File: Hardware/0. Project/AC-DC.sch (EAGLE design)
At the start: 0 parts

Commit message: Schematic design started
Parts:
- added B1, B2: (no value), rectifier:GBPC1
- added C1, C5: 15.000uF x 50V, rcl:CPOL-EUE10-35
- added C2, C6: 100nF x 50V, rcl:C-EU025-025X050
- added C3, C4, C7, C8: 10uF x 50V, rcl:CPOL-EUE3.5-8
- added D1, D2, D3, D4: 1N4007, diode:1N5060GP
- added F1: (no value), fuse:19559
- added R1, R3: (no value), rcl:R-EU_0207/7
- added R2, R4: (no value), pot:3RP/1610N
- added TR?1, TR?2: TRAFO, Trafo:TRAFO
- added U$1, U$4: AMMETER, Instrumentos:AMMETER
- added U$2, U$5: VOLTMETER, Instrumentos:VOLTMETER
- added U$3: GENERATOR, Instrumentos:GENERATOR
- added U1, U2: LM338K, REG1117:REG1117F
- added X1: (no value), con-ptr500:AK500/4-H
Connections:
- new net N$1: B1.AC1, TR?1.GRN@1
- new net N$10: F1.2, TR?1.BLK@1
- new net N$11: B2.AC1, TR?2.GRN@1
- new net N$12: B2.AC2, TR?2.GRN@2
- new net N$13: B2.+, C5.+, C6.1, D4.C, U2.VIN
- new net N$14: B2.-, C5.-, C6.2, C7.-, C8.-, R4.A, R4.S, U$5.P$2, X1-3.KL
- new net N$15: C8.+, D3.C, D4.A, R3.2, U$4.P$3, U2.VOUT
- new net N$16: C7.+, D3.A, R3.1, R4.E, U2.GND
- new net N$17: U$4.P$2, U$5.P$3, X1-4.KL
- new net N$18: TR?2.GRN/YEL1
- new net N$19: TR?2.BLK@1
- new net N$2: B1.AC2, TR?1.GRN@2
- new net N$3: B1.+, C1.+, C2.1, D2.C, U1.VIN
- new net N$4: B1.-, C1.-, C2.2, C3.-, C4.-, R2.A, R2.S, U$2.P$2, X1-2.KL
- new net N$5: C4.+, D1.C, D2.A, R1.2, U$1.P$3, U1.VOUT
- new net N$6: C3.+, D1.A, R1.1, R2.E, U1.GND
- new net N$7: U$1.P$2, U$2.P$3, X1-1.KL
- new net N$8: F1.1, U$3.P$3
- new net N$9: TR?1.GRN/YEL1, U$3.P$2

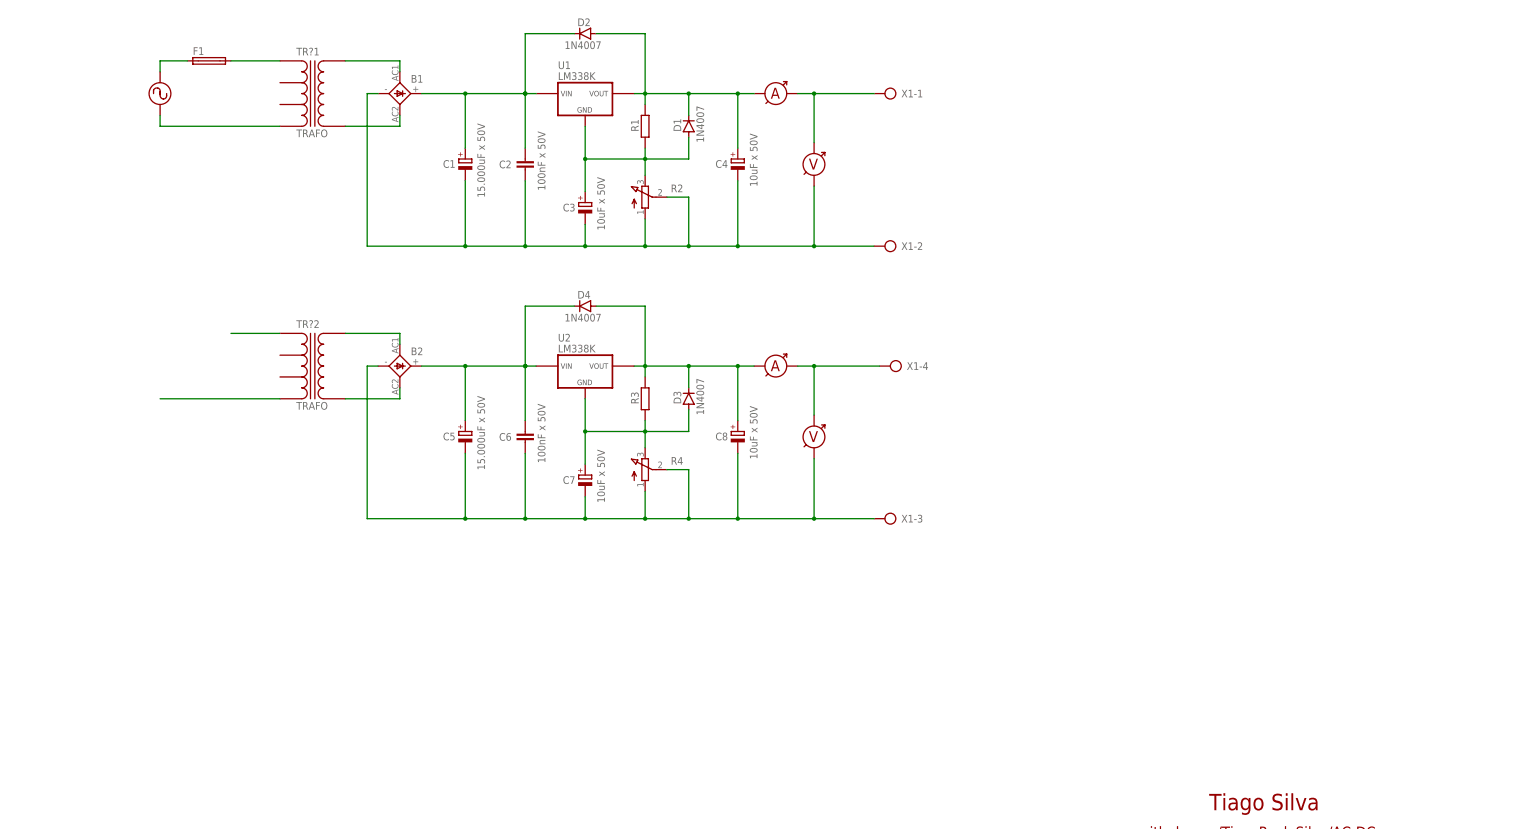
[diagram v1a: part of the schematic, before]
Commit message: Short-circuit added to schematic
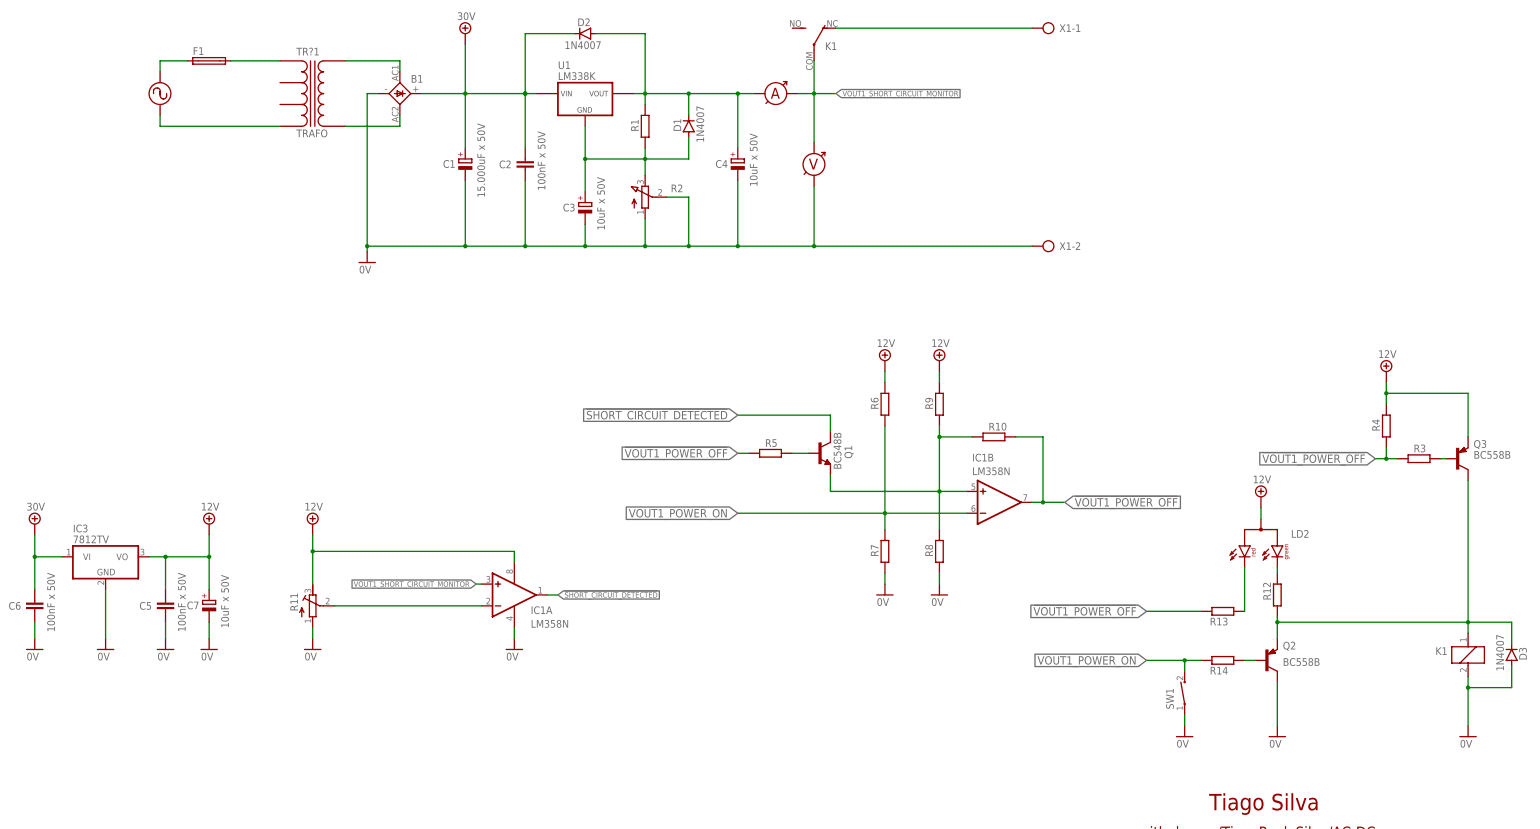
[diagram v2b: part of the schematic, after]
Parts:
- removed B2: (no value), rectifier:GBPC1
- removed C8: 10uF x 50V, rcl:CPOL-EUE3.5-8
- removed D4: 1N4007, diode:1N5060GP
- removed TR?2: TRAFO, Trafo:TRAFO
- removed U$4: AMMETER, Instrumentos:AMMETER
- removed U$5: VOLTMETER, Instrumentos:VOLTMETER
- removed U2: LM338K, REG1117:REG1117F
- added IC1: LM358N, linear:LM358N
- added IC3: 7812TV, linear:7812TV
- added K1: APF30212C, relay:APF30212C
- added LD2: (no value), led:DUOLED-RG-A
- added Q1: BC548B, transistor-npn:BC548B
- added Q2, Q3: BC558B, transistor-pnp:BC558B
- added R10, R12, R13, R14, R5, R6, R7, R8, R9: (no value), rcl:R-EU_0207/7
- added R11: (no value), rcl:R-TRIMM64W
- added SW1: CT10-XXXX-A2, switch-coto:CT10-XXXX-A2
- C5: value 15.000uF x 50V -> 100nF x 50V; device rcl:CPOL-EUE10-35 -> rcl:C-EU025-025X050
- R4: device pot:3RP/1610N -> rcl:R-EU_0207/7
- TR?1: device Trafo:TRAFO -> trafo:TRAFO
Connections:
- removed net N$15: C8.+, D3.C, D4.A, R3.2, U$4.P$3, U2.VOUT
- removed net N$16: C7.+, D3.A, R3.1, R4.E, U2.GND
- removed net N$17: U$4.P$2, U$5.P$3, X1-4.KL
- removed net N$18: TR?2.GRN/YEL1
- removed net N$19: TR?2.BLK@1
- removed net N$3: B1.+, C1.+, C2.1, D2.C, U1.VIN
- new net !SHORT_CIRCUIT_DETECTED!: IC1A.OUT, Q1.C
- new net !VOUT1_POWER_OFF!: IC1B.OUT, R10.2, R13.2, R3.1, R4.1, R5.1
- new net +24V: B1.+, C1.+, C2.1, C5.1, C6.1, C7.+, D2.C, IC1P.V+, IC3.VI, IC3.VO, LD2.A, Q3.E, R11.E, R4.2, R6.2, R9.2, U1.VIN
- new net 0V: B1.-, C1.-, C2.2, C3.-, C4.-, C5.2, C6.2, C7.-, D3.A, IC1P.V-, IC3.GND, K11.2, Q2.C, R11.A, R2.A, R2.S, R7.1, R8.1, SW1.1, U$2.P$2, X1-2.KL
- new net N$21: IC1B.+IN, Q1.E, R10.1, R8.2, R9.1
- new net N$22: Q1.B, R5.2
- new net N$25: IC1A.-IN, R11.S
- new net VOUT1_POWER_ON: IC1B.-IN, R14.2, R6.1, R7.2, SW1.2
- new net VOUT1_SHORT_CIRCUIT_MONITOR: IC1A.+IN, K12.P, U$1.P$2, U$2.P$3
- net N$11: now also LD2.CR, R13.1; no longer B2.AC1, TR?2.GRN@1
- net N$12: now also D3.C, K11.1, Q2.E, Q3.C, R12.1; no longer B2.AC2, TR?2.GRN@2
- net N$13: now also LD2.CG, R12.2; no longer B2.+, C5.+, C6.1, D4.C, U2.VIN
- net N$14: now also Q2.B, R14.1; no longer B2.-, C5.-, C6.2, C7.-, C8.-, R4.A, R4.S, U$5.P$2, X1-3.KL
- net N$4: now also K12.O, X1-1.KL; no longer B1.-, C1.-, C2.2, C3.-, C4.-, R2.A, R2.S, U$2.P$2, X1-2.KL
- net N$7: now also Q3.B, R3.2; no longer U$1.P$2, U$2.P$3, X1-1.KL
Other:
- note added: "VREF = 1.20V"
- moved on the sheet: C6, C7, D3, R3, X1-1, X1-2

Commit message: sch
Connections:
- net VOUT1_POWER_ON renamed !VOUT1_POWER_ON!
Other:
- moved on the sheet: D3, IC1B, K1, LD2, Q1, Q2, Q3, R10, R12, R13, R14, R3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

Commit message: Schematic done
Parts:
- removed IC3: 7812TV, linear:7812TV
- removed LD2: (no value), led:DUOLED-RG-A
- removed U$1: AMMETER, Instrumentos:AMMETER
- removed U$2: VOLTMETER, Instrumentos:VOLTMETER
- removed U$3: GENERATOR, Instrumentos:GENERATOR
- added AMP1, AMP2: AMMETER, Instrumentos:AMMETER
- added B2: (no value), rectifier:GBPC1
- added C10, C11: 10uF x 50V, rcl:CPOL-EUE3.5-8
- added C8: 15.000uF x 50V, rcl:CPOL-EUE10-35
- added C9: 100nF x 50V, rcl:C-EU025-025X050
- added D4, D5: 1N4007, diode:1N5060GP
- added G1: GENERATOR, Instrumentos:GENERATOR
- added IC2: LM358N, linear:LM358N
- added K2, K3: 12VDC, relay:APF30212C
- added LD1: (no value), led:DUOLED-RG-A
- added R15: 5K, pot:3RP/1610N
- added R16: 100k (5%), rcl:R-EU_0207/7
- added R17: 10k (5%), rcl:R-EU_0207/7
- added S1: (no value), switch:320-938
- added TR?2: TRAFO, Trafo:TRAFO
- added U2: LM338K, REG1117:REG1117F
- added VOLT1, VOLT2: VOLTMETER, Instrumentos:VOLTMETER
- added X2: (no value), con-ptr500:AK500/4-H
- C1: value 15.000uF x 50V -> 100nF x 50V; device rcl:CPOL-EUE10-35 -> rcl:C-EU025-025X050
- C4: value 10uF x 50V -> 15.000uF x 50V; device rcl:CPOL-EUE3.5-8 -> rcl:CPOL-EUE10-35
- C6: value 100nF x 50V -> 10uF x 50V; device rcl:C-EU025-025X050 -> rcl:CPOL-EUE3.5-8
- IC1: value LM358N -> 7812TV; device linear:LM358N -> linear:7812TV
- R1: value (none) -> VARISTOR-2,5; device rcl:R-EU_0207/7 -> varistor:VARISTOR-2,5
- R10: value (none) -> 220k (5%)
- R11: value (none) -> 1k (5%); device rcl:R-TRIMM64W -> rcl:R-EU_0207/7
- R12, R5: value (none) -> 10k (5%)
- R13: value (none) -> 100R (5%)
- R14, R3: value (none) -> 500R; device rcl:R-EU_0207/7 -> rcl:R-TRIMMT93YB
- R2: value (none) -> 300k; device pot:3RP/1610N -> rcl:R-TRIMM64W
- R4: value (none) -> 5K; device rcl:R-EU_0207/7 -> pot:3RP/1610N
- R6, R7, R8, R9: value (none) -> 100k (5%)
- TR?1: device trafo:TRAFO -> Trafo:TRAFO
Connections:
- removed net +24V: B1.+, C1.+, C2.1, C5.1, C6.1, C7.+, D2.C, IC1P.V+, IC3.VI, IC3.VO, LD2.A, Q3.E, R11.E, R4.2, R6.2, R9.2, U1.VIN
- removed net N$10 (its old number): F1.2, TR?1.BLK@1
- removed net N$11 (its old number): LD2.CR, R13.1
- new net 0V_A: G1.P$2, R1.2, S1B.O, TR?1.GRN/YEL1, TR?2.GRN/YEL1
- new net 0V_B: S1B.P, TR?1.GRN/YEL, TR?2.GRN/YEL
- new net 127V_A: F1.2, R1.1, S11.O, TR?1.BLK@1, TR?2.BLK@1
- new net 127V_B: S11.P, TR?1.BLK@2, TR?2.BLK@2
- new net 12V: C2.1, C3.+, IC1.VO, IC2P.V+, LD1.A, Q3.E, R16.2, R2.E, R6.2, R8.2
- new net 30V: B1.+, B2.+, C1.1, C4.+, C5.1, C8.+, C9.1, D1.C, D3.C, IC1.VI, U1.VIN, U2.VIN
- new net N$1: B2.AC1, TR?2.GRN@1
- new net N$15: AMP1.P$3, C7.+, D1.A, D2.C, R3.E, U1.VOUT
- new net N$16: C6.+, D2.A, R3.A, R3.S, R4.E, U1.GND
- new net N$2: B2.AC2, TR?2.GRN@2
- new net N$3: LD1.CR, R11.1
- new net N$4: K32.O, X2-1.KL
- net !SHORT_CIRCUIT_DETECTED!: now also IC2A.OUT; no longer IC1A.OUT
- net !VOUT1_POWER_OFF!: now also IC2B.OUT, R11.2, R16.1, R17.1; no longer IC1B.OUT, R13.2, R3.1, R4.1
- net !VOUT1_POWER_ON!: now also IC2B.-IN, R12.2; no longer IC1B.-IN, R14.2
- net 0V: now also B2.-, C1.2, C10.-, C11.-, C6.-, C8.-, C9.2, D5.A, IC1.GND, IC2P.V-, K21.2, K31.2, R15.A, R15.S, R4.A, R4.S, R9.1, VOLT1.P$2, VOLT2.P$2, X2-2.KL; no longer C1.-, C6.2, D3.A, IC1P.V-, IC3.GND, K11.2, R11.A, R2.S, R8.1, U$2.P$2
- net N$12: now also D5.C, K21.1, K31.1, R13.1; no longer D3.C, K11.1, R12.1
- net N$13: now also LD1.CG, R13.2; no longer LD2.CG, R12.2
- net N$14: now also R12.1; no longer R14.1
- net N$21: now also IC2B.+IN, R8.1, R9.2; no longer IC1B.+IN, R8.2, R9.1
- net N$25: now also IC2A.-IN, R2.S; no longer IC1A.-IN, R11.S
- net N$5: now also AMP2.P$3, C11.+, D3.A, D4.C, R14.E, U2.VOUT; no longer C4.+, D1.C, D2.A, R1.2, U$1.P$3, U1.VOUT
- net N$6: now also C10.+, D4.A, R14.A, R14.S, R15.E, U2.GND; no longer C3.+, D1.A, R1.1, R2.E, U1.GND
- net N$7: now also R17.2; no longer R3.2
- net N$8: now also G1.P$3; no longer U$3.P$3
- net N$9: now also S11.S, S1B.S; no longer TR?1.GRN/YEL1, U$3.P$2
- net VOUT1_SHORT_CIRCUIT_MONITOR: now also AMP1.P$2, AMP2.P$2, IC2A.+IN, K32.P, VOLT1.P$3, VOLT2.P$3; no longer IC1A.+IN, U$1.P$2, U$2.P$3
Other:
- note added: "127V OR 220V AC INPUTY SELECT"
- note added: "AUXILIARY FIXED POWER SUPPLY"
- note added: "OUTPUT ON/OFF DRIVER"
- note added: "OUTPUT ON/OFF TRIGGER WITH LATCH"
- note added: "OUTPUT STATUS USER INTERFACE"
- note added: "POWER SUPPLY 1"
- note added: "POWER SUPPLY 2"
- note added: "SHORT CIRCUIT MONITOR"
- moved on the sheet: B1, C2, C3, C4, C5, C7, D1, D2, D3, F1, K1, Q1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

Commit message: Inrush current's capacitor circuit protect added
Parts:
- removed IC2: LM358N, linear:LM358N
- added D6, D7, D8: 1N4007, diode:1N5060GP
- added IC3: LM324N, linear:LM324N
- added K4, K7: 12VDC, relay:APF30212C
- added K5: APF30212C, relay:APF30212C
- added KK1, KK2: D0A-L, heatsink:D0A-L
- added R18: 10k (5%), rcl:R-EU_0207/7
- added R19: 500k, rcl:R-TRIMM64W
- added R20: 100k (1%), rcl:R-EU_0207/7
- added R21: 33k (1%), rcl:R-EU_0207/7
- added R22: 5K, pot:3RP/1610N
- added R23: 500R, rcl:R-TRIMMT93YB
- added R24: 5R, ptc-ntc:NTC640
- added T1: BC337, transistor-neu-to92:BC337
- B1, B2: value (none) -> KBPC608
- LD1: value (none) -> Bicolor AC (Red/Green)
- R14: value 500R -> 5R; device rcl:R-TRIMMT93YB -> ptc-ntc:NTC640
- R15: value 5K -> 10k (5%); device pot:3RP/1610N -> rcl:R-EU_0207/7
- R2: value 300k -> 500k
- R6, R7, R8, R9: value 100k (5%) -> 100k (1%)
- S1: value (none) -> HH 6T
- TR?1, TR?2: value TRAFO -> 24V @ 5A
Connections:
- removed net VOUT1_SHORT_CIRCUIT_MONITOR: AMP1.P$2, AMP2.P$2, IC2A.+IN, K12.P, K32.P, VOLT1.P$3, VOLT2.P$3
- new net +24V: D6.C, IC3P.V+, K41.1, K71.1, R19.E, R20.2
- new net N$1: B1.+, K42.P, R14.2
- new net N$18: IC3C.+IN, R20.1, R21.2
- new net N$19: D3.A, IC3A.OUT
- new net N$2: D6.A, K41.2, K71.2, T1.C
- new net N$20: D4.A, IC3D.OUT
- new net N$26: AMP2.P$3, C11.+, D5.C, D8.A, R23.E, U2.VOUT
- new net N$27: C10.+, D5.A, R22.E, R23.A, R23.S, U2.GND
- new net N$28: K52.O, X2-1.KL
- new net N$29: B2.+, K72.P, R24.2
- new net SHORT_CIRCUIT_MONITOR_1: AMP1.P$2, AMP2.P$2, IC3A.+IN, K12.P, K52.P, VOLT1.P$3, VOLT2.P$3
- new net SHORT_CIRCUIT_MONITOR_2: IC3D.+IN
- net !SHORT_CIRCUIT_DETECTED!: now also D3.C, D4.C; no longer IC2A.OUT
- net !VOUT1_POWER_OFF!: now also IC3B.OUT; no longer IC2B.OUT
- net !VOUT1_POWER_ON!: now also IC3B.-IN; no longer IC2B.-IN
- net 0V: now also D7.A, IC3P.V-, R18.1, R19.A, R21.1, R22.A, R22.S, T1.E; no longer D5.A, IC2P.V-, R15.A, R15.S
- net 12V: no longer IC2P.V+
- net 30V: now also D8.C, K42.S, K72.S, R14.1, R24.1; no longer B1.+, B2.+, D3.C
- net N$12: now also D7.C; no longer D5.C
- net N$21: now also IC3B.+IN; no longer IC2B.+IN
- net N$25: now also IC3A.-IN, IC3D.-IN; no longer IC2A.-IN
- net N$4: now also R15.2, T1.B; no longer K32.O, X2-1.KL
- net N$5: now also IC3C.OUT, R15.1, R18.2; no longer AMP2.P$3, C11.+, D3.A, D4.C, R14.E, U2.VOUT
- net N$6: now also IC3C.-IN, R19.S; no longer C10.+, D4.A, R14.A, R14.S, R15.E, U2.GND
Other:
- note added: "THERMISTOR FAST TEMPERATURE RECOVERY"
- moved on the sheet: B1, B2, C1, C10, C11, C2, C3, C4, C5, C6, C7, C8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

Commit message: Temperature Sensor for Heat Sink Added
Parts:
- removed C1: 100nF x 50V, rcl:C-EU025-025X050
- added C12, C13: 100nF x 50V, rcl:C-EU025-025X050
- added C14: 10uF x 50V, rcl:CPOL-EUE3.5-8
- added D10: 1N4007, diode:1N5060GP
- added IC2: 7824TV, linear:7824TV
- added IC4: LM358N, linear:LM358N
- added L2: Cooler 24V @ 6W, Inductor:INDUCTOR
- added Q4, Q5: BC558B, transistor-pnp:BC558B
- added R25, R26, R29, R34: 100k (5%), rcl:R-EU_0207/7
- added R27, R28: 10k, ptc-ntc:NTC640
- added R30, R31, R32, R33: 10k, rcl:R-TRIMM64W
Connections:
- new net HIGH_TEMPERATURE_1: IC4A.OUT, R29.2, R34.1
- new net HIGH_TEMPERATURE_2: IC4B.OUT, R25.2, R26.1
- new net N$30: IC4B.+IN, R25.1, R33.S
- new net N$31: IC4B.-IN, R27.1, R32.E, R32.S
- new net N$32: Q5.B, R34.2
- new net N$34: Q4.B, R26.2
- new net N$35: IC4A.-IN, R28.1, R30.E, R30.S
- new net N$36: IC4A.+IN, R29.1, R31.S
- new net N$38: D10.C, L2.1, Q4.C, Q5.C
- net +24V: now also C12.1, C14.+, IC1.VI, IC2.VO, IC4P.V+, Q4.E, Q5.E, R27.2, R28.2, R31.E, R33.E
- net 0V: now also C12.2, C13.2, C14.-, D10.A, IC2.GND, IC4P.V-, L2.2, R30.A, R31.A, R32.A, R33.A; no longer C1.2
- net 30V: now also C13.1, IC2.VI; no longer C1.1, IC1.VI
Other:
- note added: "COOLER ON/OFF DRIVER"
- note added: "FIXED AUXILIARY POWER SUPPLIES"
- note added: "TEMPERATURE MONITOR VOLTAGE REGULATOR 1"
- note added: "TEMPERATURE MONITOR VOLTAGE REGULATOR 2"
- note removed: "AUXILIARY FIXED POWER SUPPLY"
- moved on the sheet: B1, B2, C10, C11, C2, C3, C4, C5, C6, C7, C8, C9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
